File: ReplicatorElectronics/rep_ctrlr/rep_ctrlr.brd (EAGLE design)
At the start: 106.5 x 89 mm, 98 parts, among them IC1 MICROCHIP_PIC32MX7X5F256L-PF, IC2 MICROCHIP_MCP6001-LT, IC3 MICROCHIP_MCP6001-LT, IC4 MICROCHIP_MCP6001-LT, IC5 MICROCHIP_MCP6001-LT, J1 ATX24RH, J10 SBH11-PBPC-D07-ST-BK, J11 SBH11-PBPC-D07-ST-BK, J12 SBH11-PBPC-D07-ST-BK, J13 SBH11-PBPC-D07-ST-BK, J14 SBH11-PBPC-D07-ST-BK, J15 SBH11-PBPC-D07-ST-BK, J16 SBH11-PBPC-D07-ST-BK, J17 SBH11-PBPC-D07-ST-BK, J18 SI-50170-F, J19 70553-0106, J4 RJ11-2L-B, J6 SBH11-PBPC-D05-ST-BK, J7 SBH11-PBPC-D05-ST-BK, J8 SBH11-PBPC-D05-ST-BK, J9 SBH11-PBPC-D05-ST-BK, Q1 ASFL1, Q2 ASFL1, U18 LDS3985XX33

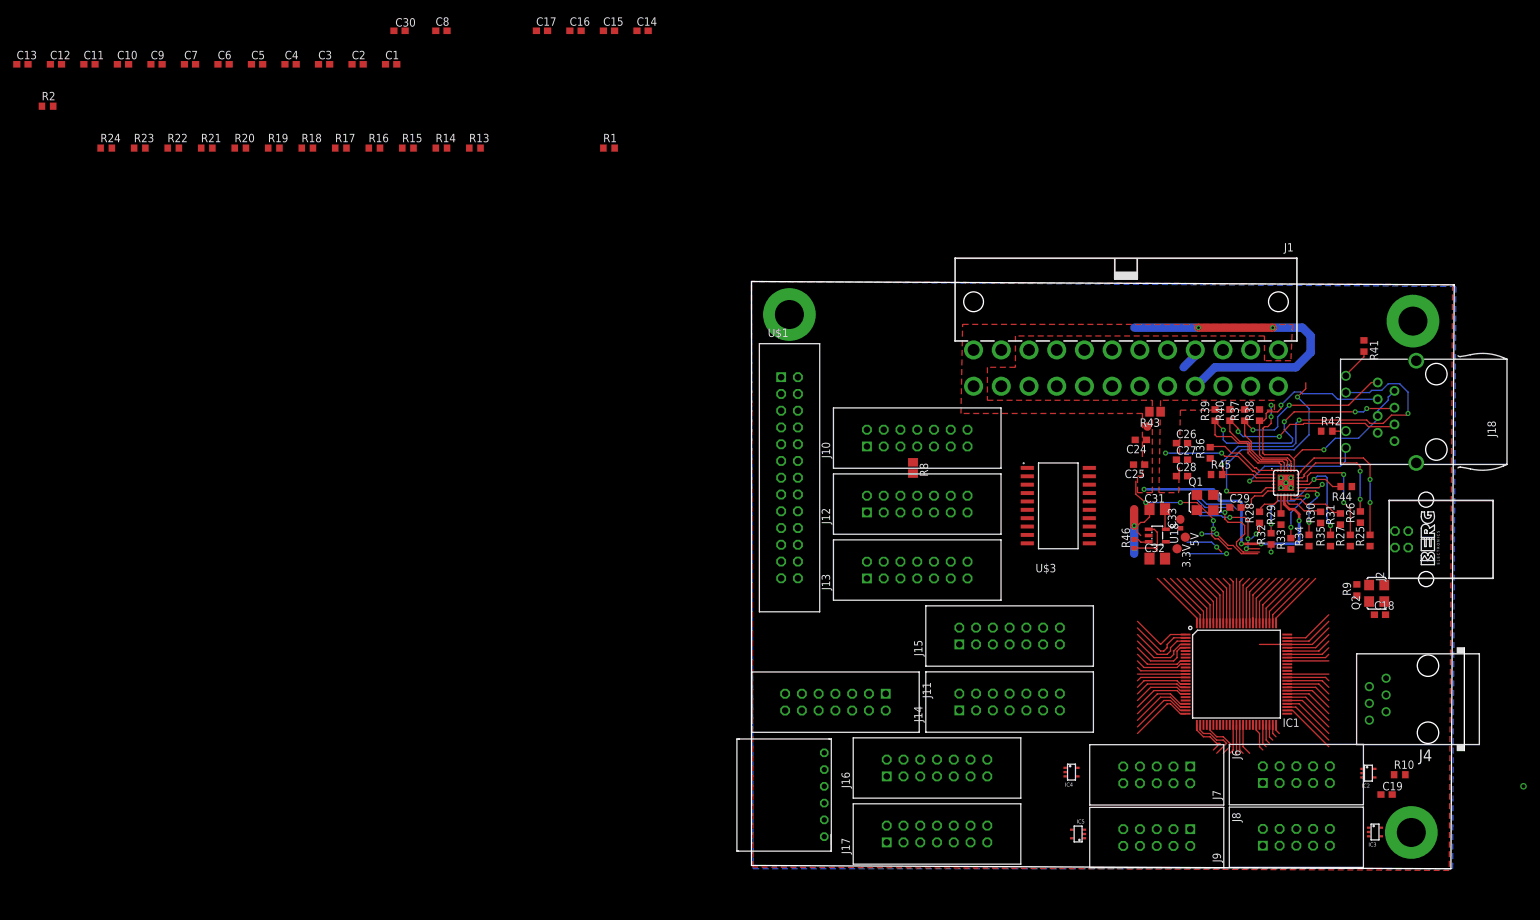
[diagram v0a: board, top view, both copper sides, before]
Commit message: 5/14/12: Began power rail routing and display connector routing.
~ 2 hrs
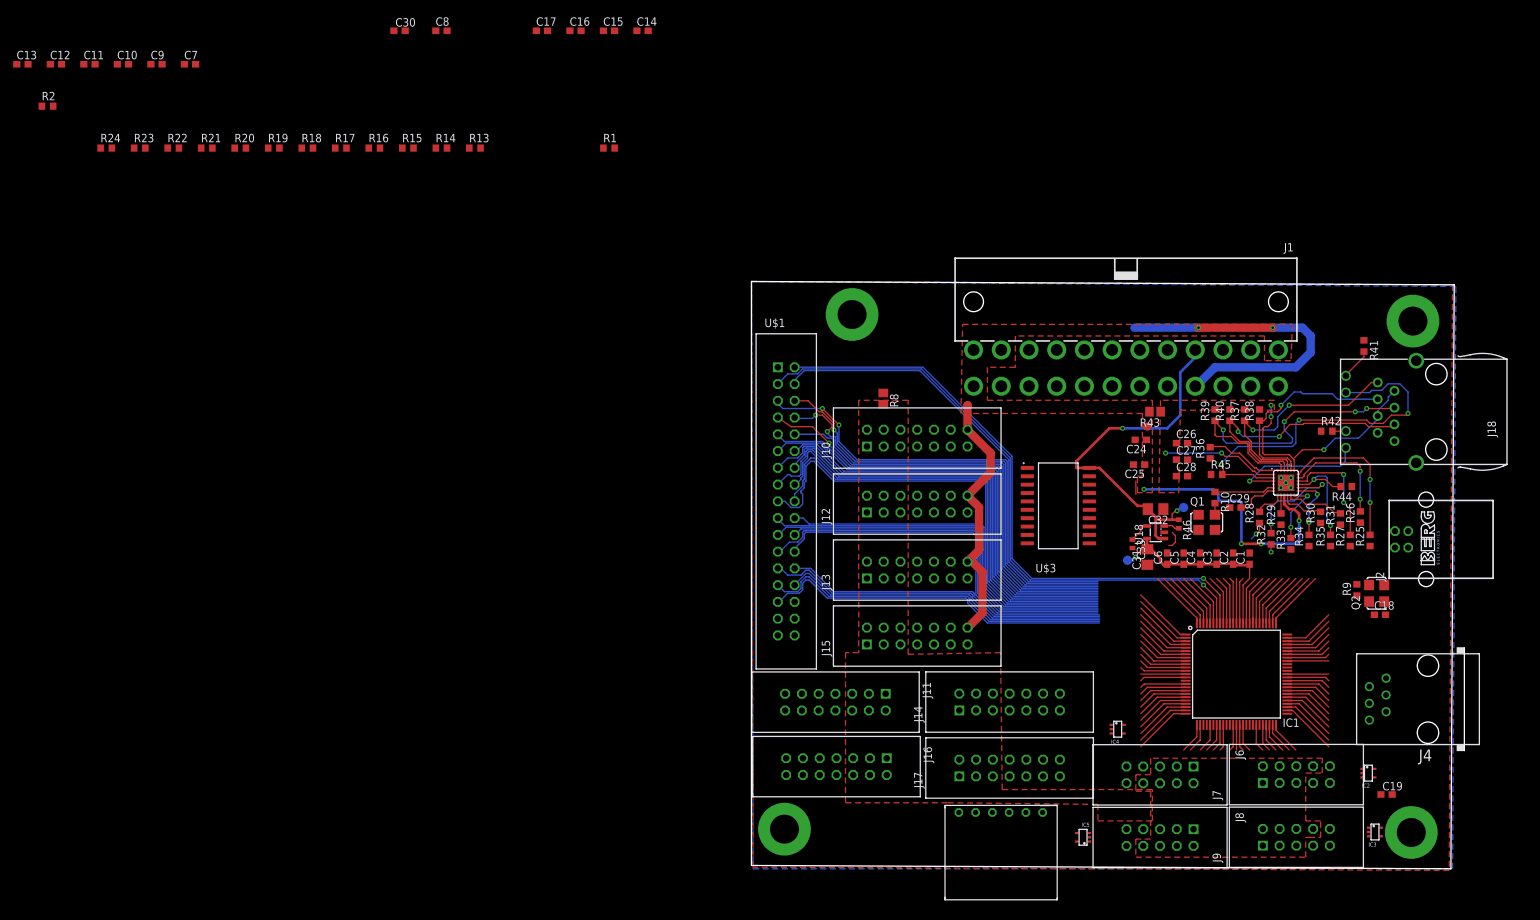
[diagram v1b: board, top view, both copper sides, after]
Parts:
- U$1: value SBH11-PBPC-D13-ST-BK -> SBH11-PBPC-D17-ST-BK; device SBH11-PBPC-D13-ST-BK:SBH11-PBPC-D13-ST-BK -> SBH11-PBPC-D17-ST-BK:SBH11-PBPC-D17-ST-BK
- moved C6 161.4 mm to (63.0, 47.0), turned to 90 degrees
- moved C5 159.2 mm to (65.5, 47.0), turned to 90 degrees
- moved C4 156.9 mm to (68.0, 47.0), turned to 90 degrees
- moved C3 154.6 mm to (70.5, 47.0), turned to 90 degrees
- moved C2 152.4 mm to (73.0, 47.0), turned to 90 degrees
- moved C1 150.1 mm to (75.5, 47.0), turned to 90 degrees
- moved R10 50.5 mm to (70.2, 56.2), turned to 270 degrees
- moved J19 31.9 mm to (36.5, 3.45), turned to 90 degrees
- moved J17 14.9 mm to (31.5, 14.0)
- moved J15 14.0 mm to (17.5, 34.0)
- moved R8 11.4 mm to (20.0, 71.2)
- moved IC4 9.55 mm to (55.5, 21.1)
- moved C33 7.85 mm to (57.8, 49.2), turned to 270 degrees
- moved 3.3V 7.70 mm to (57.0, 46.8), flipped to the bottom
- moved C32 7.50 mm to (61.2, 54.5), turned to 180 degrees
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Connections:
- removed net ETXERR: IC1.35
- removed net PICCLKO: IC1.64
- net +3V3: now also C1.1, C18.1, C2.1, C3.1, C4.1, C5.1, C6.1, IC1.16, IC1.2, IC1.37, IC1.46, IC1.55, IC1.62, IC1.86, Q2.4, R1.2, R2.2
- net DGND: now also U$1.30, U$1.32; no longer U$1.22, U$1.24, U$1.26
- net HEAT0_ON: now also IC1.11
- net LCD_CS: now also U$1.22
- net LCD_RD: now also U$1.23
- net LCD_RST: now also U$1.25
- net LCD_WR: now also U$1.24
- net SD_CSN: now also U$1.26; no longer U$1.18
- net SD_SP_MISO: now also U$1.29; no longer U$1.20
- net SD_SP_MOSI: now also U$1.28; no longer U$1.21
- net SD_SP_SCK: now also U$1.27; no longer U$1.19
- net VCC: now also U$1.31, U$1.33; no longer C1.1, C18.1, C2.1, C3.1, C4.1, C5.1, C6.1, IC1.16, IC1.2, IC1.37, IC1.46, IC1.55, IC1.62, IC1.86, Q2.4, R1.2, R2.2, U$1.23, U$1.25
- net X+: now also U$1.18
- net X-: now also U$1.19
- net Y+: now also U$1.20
- net Y-: now also U$1.21
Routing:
- net DB1: track 8.04 -> 94.7 mm, vias 0 -> 1
- net DB0: track 7.84 -> 92.1 mm, vias 0 -> 1
- net X+: track 0.00 -> 77.3 mm
- net DB17: track 7.63 -> 80.8 mm
- net DB15: track 8.46 -> 79.5 mm
- net DB3: track 9.08 -> 79.8 mm, vias 0 -> 2
- net DB2: track 8.87 -> 78.4 mm
- net DB13: track 7.01 -> 75.8 mm
- net LCD_RD: track 0.00 -> 68.8 mm
- net DB16: track 8.64 -> 76.9 mm
- net DB4: track 9.29 -> 77.4 mm, vias 0 -> 1
- net +3V3: track 3.10 -> 70.9 mm, vias 0 -> 1
- net DB6: track 9.46 -> 77.3 mm, vias 0 -> 2
- net DB11: track 7.01 -> 74.7 mm
- net DB5: track 9.66 -> 77.3 mm, vias 0 -> 1
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- added copper zone on layer 1, net GND

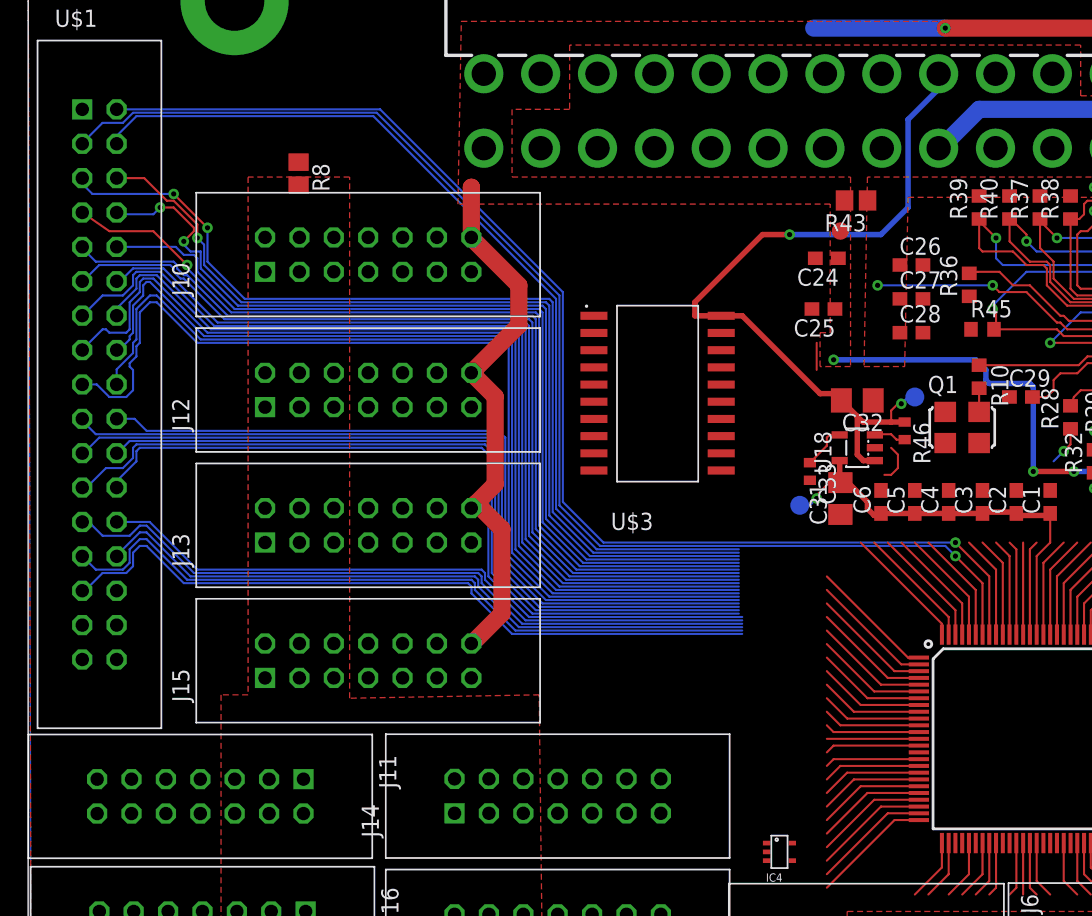
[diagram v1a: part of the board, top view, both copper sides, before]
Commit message: 5/14/12: Adjusted spacing on display connector traces.
~1 hr.
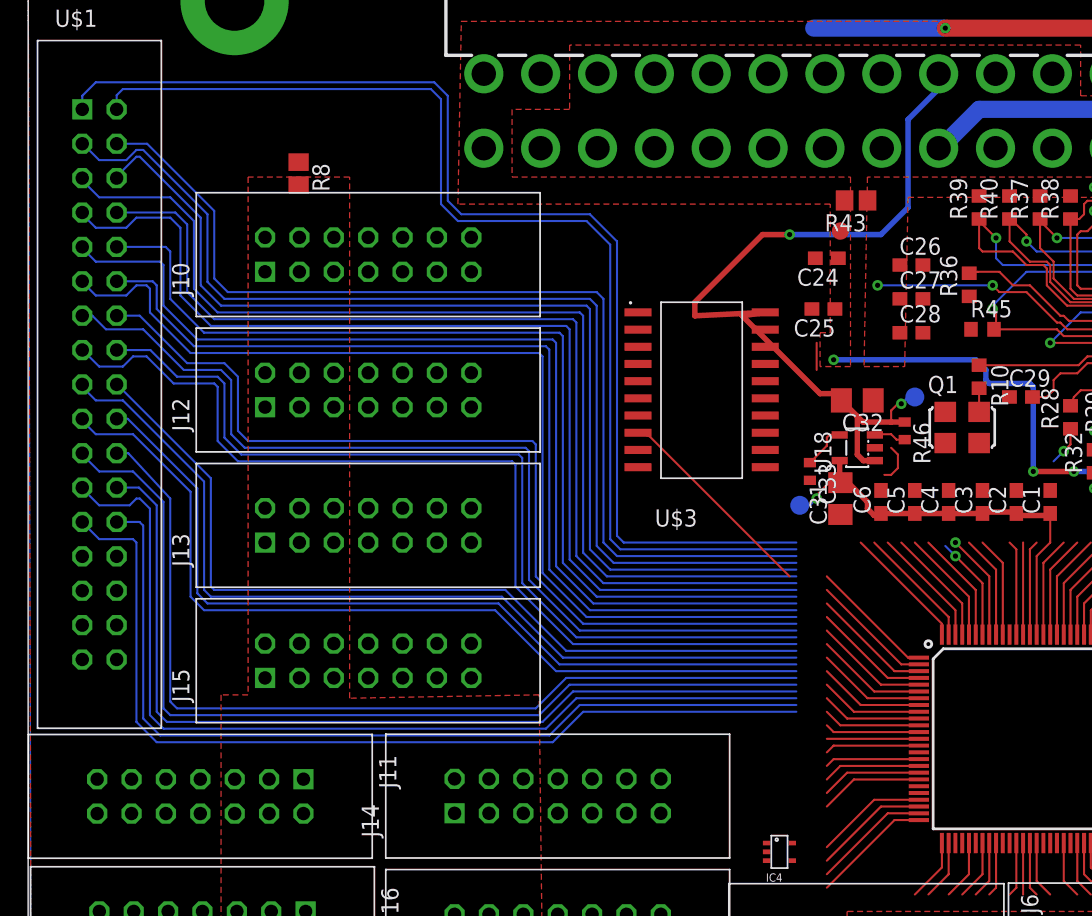
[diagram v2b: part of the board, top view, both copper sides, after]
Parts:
- moved U$3 3.26 mm to (49.8, 55.2)
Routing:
- net A0: track 4.21 -> 89.7 mm
- net SD_SP_SCK: track 57.8 -> 4.01 mm
- net SD_SP_MISO: track 58.5 -> 4.84 mm
- net SD_SP_MOSI: track 55.2 -> 5.04 mm
- net ENC_3_3V: track 79.9 -> 39.7 mm, vias 5 -> 4
- net SD_CSN: track 56.2 -> 72.7 mm
- net SERVO3: track 8.37 -> 23.9 mm
- net LCD_RST: track 60.6 -> 76.0 mm
- net X+: track 77.3 -> 63.0 mm
- net Y-: track 63.8 -> 75.1 mm
- net LCD_CS: track 60.8 -> 71.8 mm
- net LCD_RD: track 68.8 -> 78.5 mm
- net DB5: track 77.3 -> 86.8 mm, vias 1 -> 0
- net DB4: track 77.4 -> 86.2 mm, vias 1 -> 0
- net LCD_WR: track 66.8 -> 75.5 mm
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
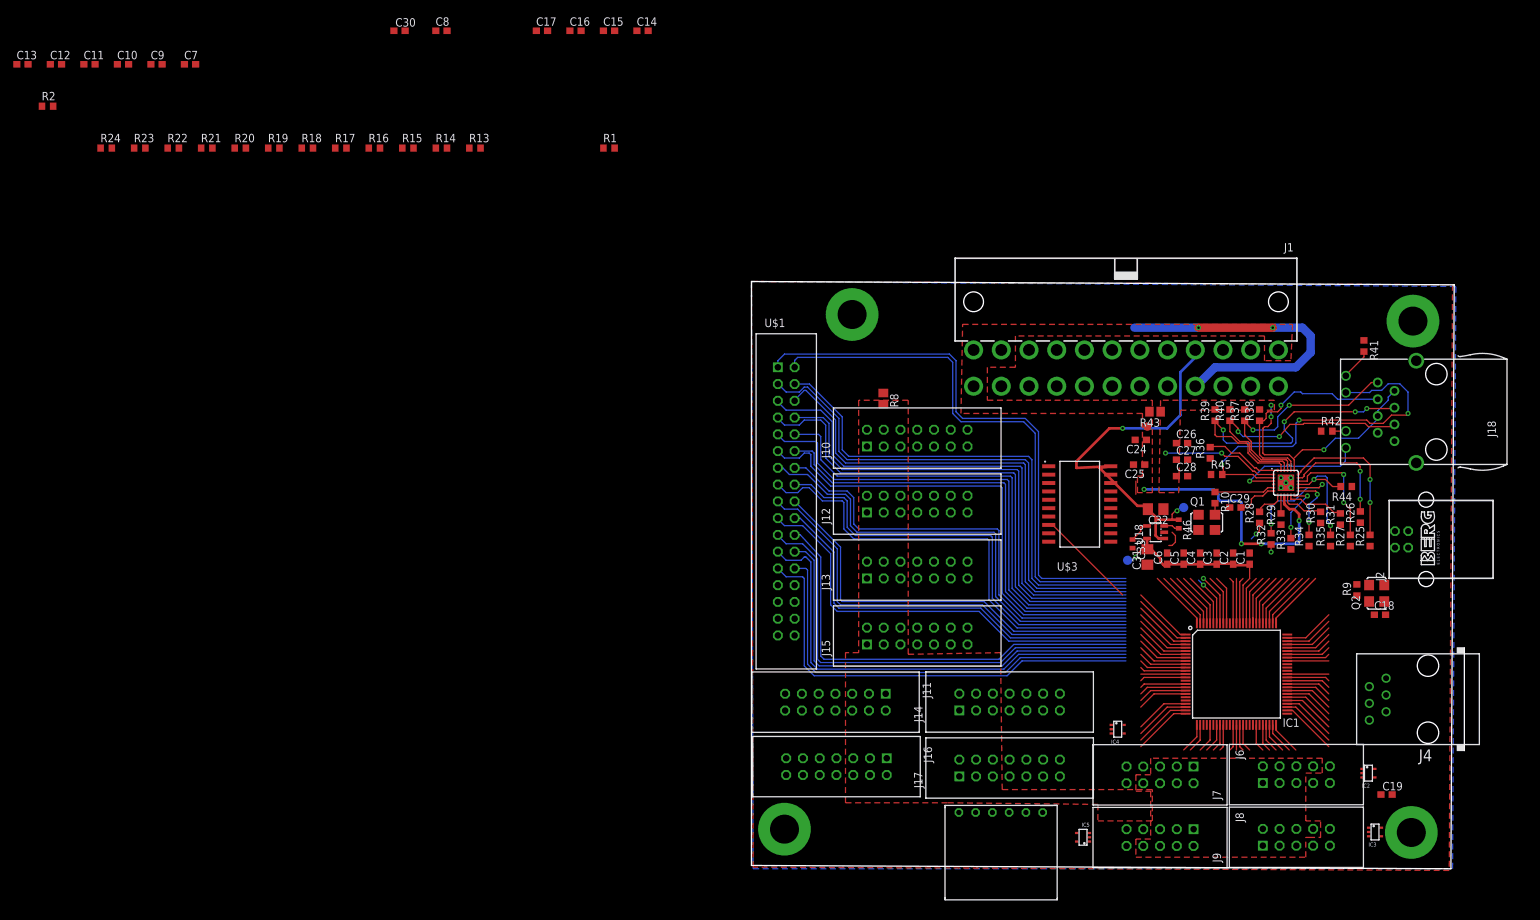
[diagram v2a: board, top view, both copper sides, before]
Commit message: 5/15/12: Completed power routing, completed servo connector routing save for PIC traces (which now lead nearby PIC but do not connect to pins). Heater connectors and PIC IO routing remain largely untouched. Some passives have yet to be placed.
~ 3 hrs.
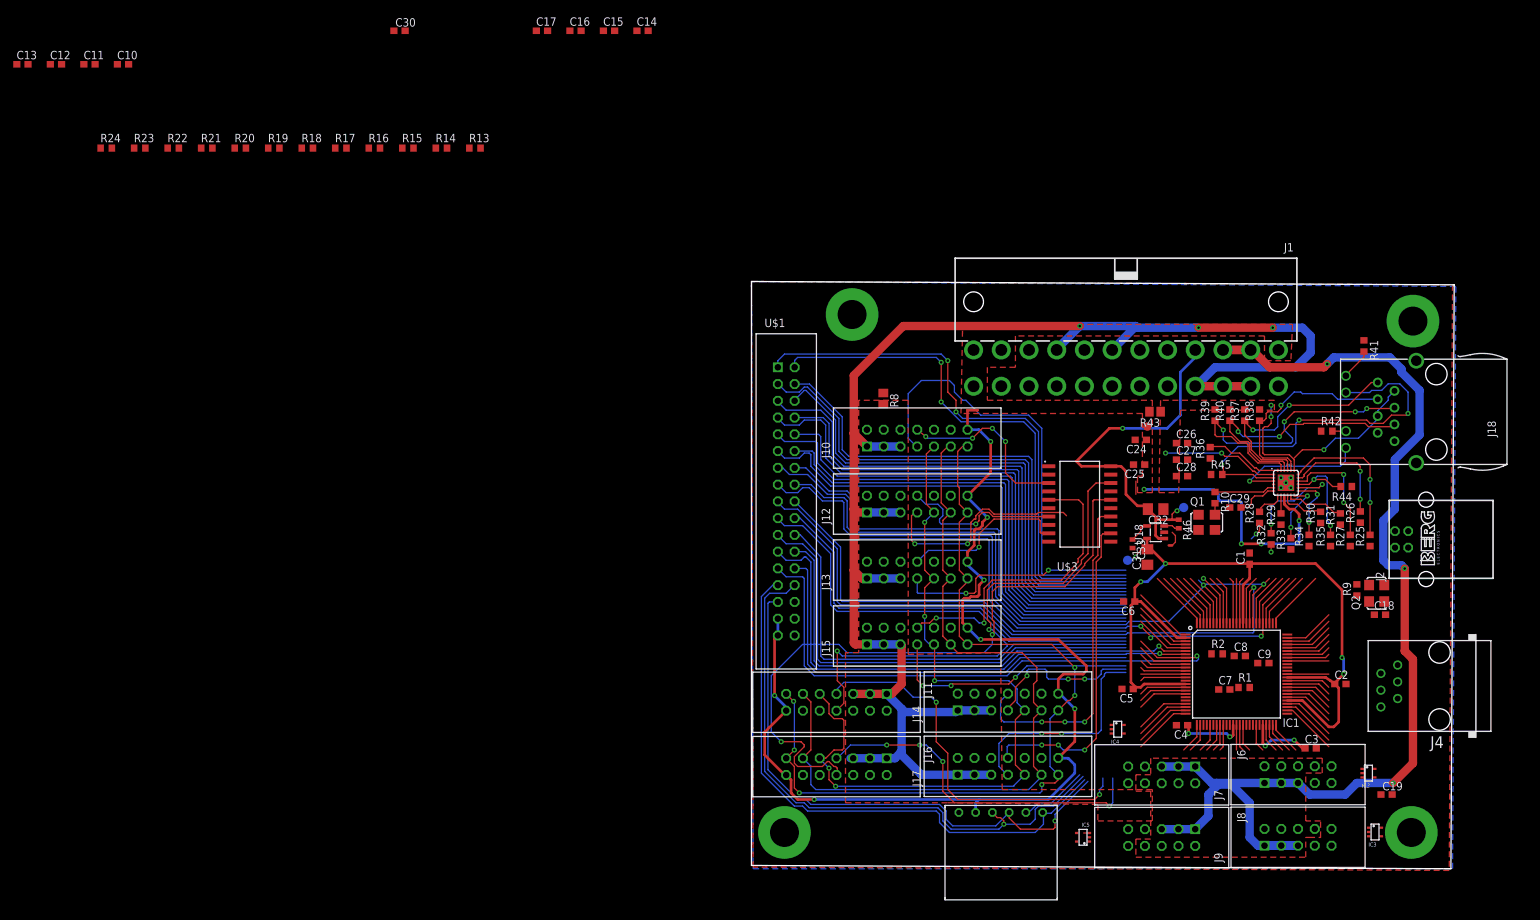
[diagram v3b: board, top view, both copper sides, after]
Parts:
- moved R2 195.7 mm to (70.6, 32.6)
- moved C9 190.7 mm to (77.6, 31.2)
- moved C7 183.2 mm to (71.7, 27.2)
- moved C8 153.7 mm to (74.0, 32.2)
- moved R1 126.3 mm to (74.7, 27.5)
- moved C3 32.1 mm to (84.8, 18.2), turned to 0 degrees
- moved C4 25.4 mm to (65.2, 21.8), turned to 180 degrees
- moved C2 25.0 mm to (89.2, 28.0), turned to 0 degrees
- moved C5 21.5 mm to (57.0, 27.2), turned to 180 degrees
- moved C6 8.68 mm to (57.2, 40.5), turned to 180 degrees
- moved J4 2.66 mm to (104.3, 27.7)
- moved J17 0.35 mm to (31.2, 14.2)
- moved J14 0.25 mm to (31.2, 24.0)
- moved J6 0.25 mm to (67.2, 15.5)
- moved J7 0.25 mm to (77.8, 13.0)
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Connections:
- net ENC_3_3V: now also J19.P$5, U$1.31, U$1.33
- net SERVO0: now also U$3.17; no longer J10.8, U$3.2
- net SERVO0_5V: now also J10.8, U$3.3; no longer U$3.18
- net SERVO1: now also U$3.2; no longer J11.8, U$3.4
- net SERVO1_5V: now also J11.8, U$3.18; no longer U$3.16
- net SERVO2: now also U$3.13; no longer J12.8, U$3.6
- net SERVO2_5V: now also J12.8, U$3.7; no longer U$3.14
- net SERVO3: now also U$3.11; no longer J13.8, U$3.8
- net SERVO3_5V: now also J13.8, U$3.9; no longer U$3.12
- net SERVO4: now also U$3.6; no longer J14.8, U$3.11
- net SERVO4_5V: now also J14.8, U$3.14; no longer U$3.9
- net SERVO5: now also U$3.15; no longer J15.8, U$3.13
- net SERVO5_5V: now also J15.8, U$3.5; no longer U$3.7
- net SERVO6: now also U$3.4; no longer J16.8, U$3.15
- net SERVO6_5V: now also J16.8, U$3.16; no longer U$3.5
- net SERVO7: now also U$3.8; no longer J17.8, U$3.17
- net SERVO7_5V: now also J17.8, U$3.12; no longer U$3.3
- net VCC: no longer J19.P$5, U$1.31, U$1.33
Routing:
- net 5V_SERVO: track 49.3 -> 245.4 mm, vias 2 -> 3
- net 12V_HEAT: track 0.00 -> 179.4 mm, vias 0 -> 3
- net ENC_3_3V: track 39.7 -> 206.6 mm, vias 4 -> 12
- net ENC_MISO: track 7.63 -> 136.0 mm, vias 0 -> 6
- net ENC_MOSI: track 7.34 -> 125.0 mm
- net ENC_SCK: track 6.92 -> 123.4 mm, vias 0 -> 5
- net SERVO6_5V: track 0.00 -> 99.7 mm, vias 0 -> 2
- net SD_SP_MOSI: track 5.04 -> 96.2 mm, vias 0 -> 1
- net SD_SP_SCK: track 4.01 -> 91.9 mm
- net SD_SP_MISO: track 4.84 -> 91.0 mm, vias 0 -> 1
- net SERVO1_5V: track 0.00 -> 78.2 mm, vias 0 -> 2
- net +3V3: track 70.9 -> 145.9 mm, vias 1 -> 9
- net ENC0_CSN: track 7.21 -> 75.4 mm
- net ENC1_CSN: track 3.80 -> 61.9 mm, vias 0 -> 2
- net ENC6_CSN: track 7.42 -> 60.5 mm, vias 0 -> 4
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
